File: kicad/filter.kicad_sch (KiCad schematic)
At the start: 21 parts, among them Q19 BC547, Q20 BC557, U1 NE5532

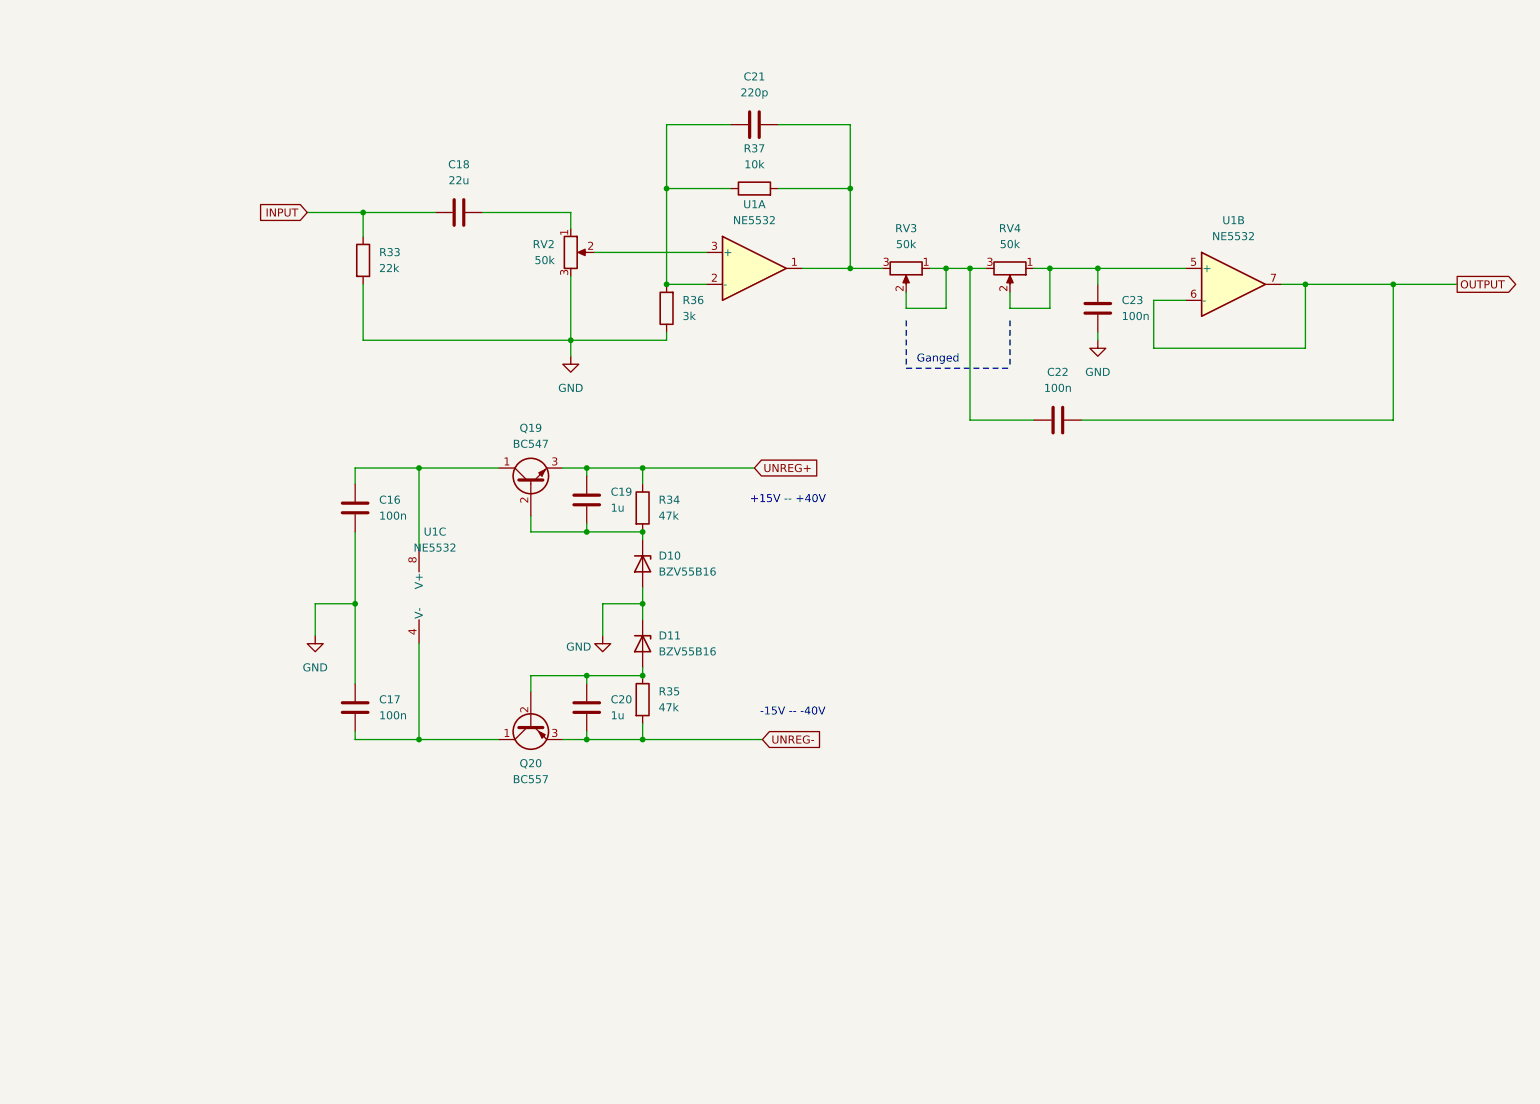
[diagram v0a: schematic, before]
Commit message: Added preamp sim
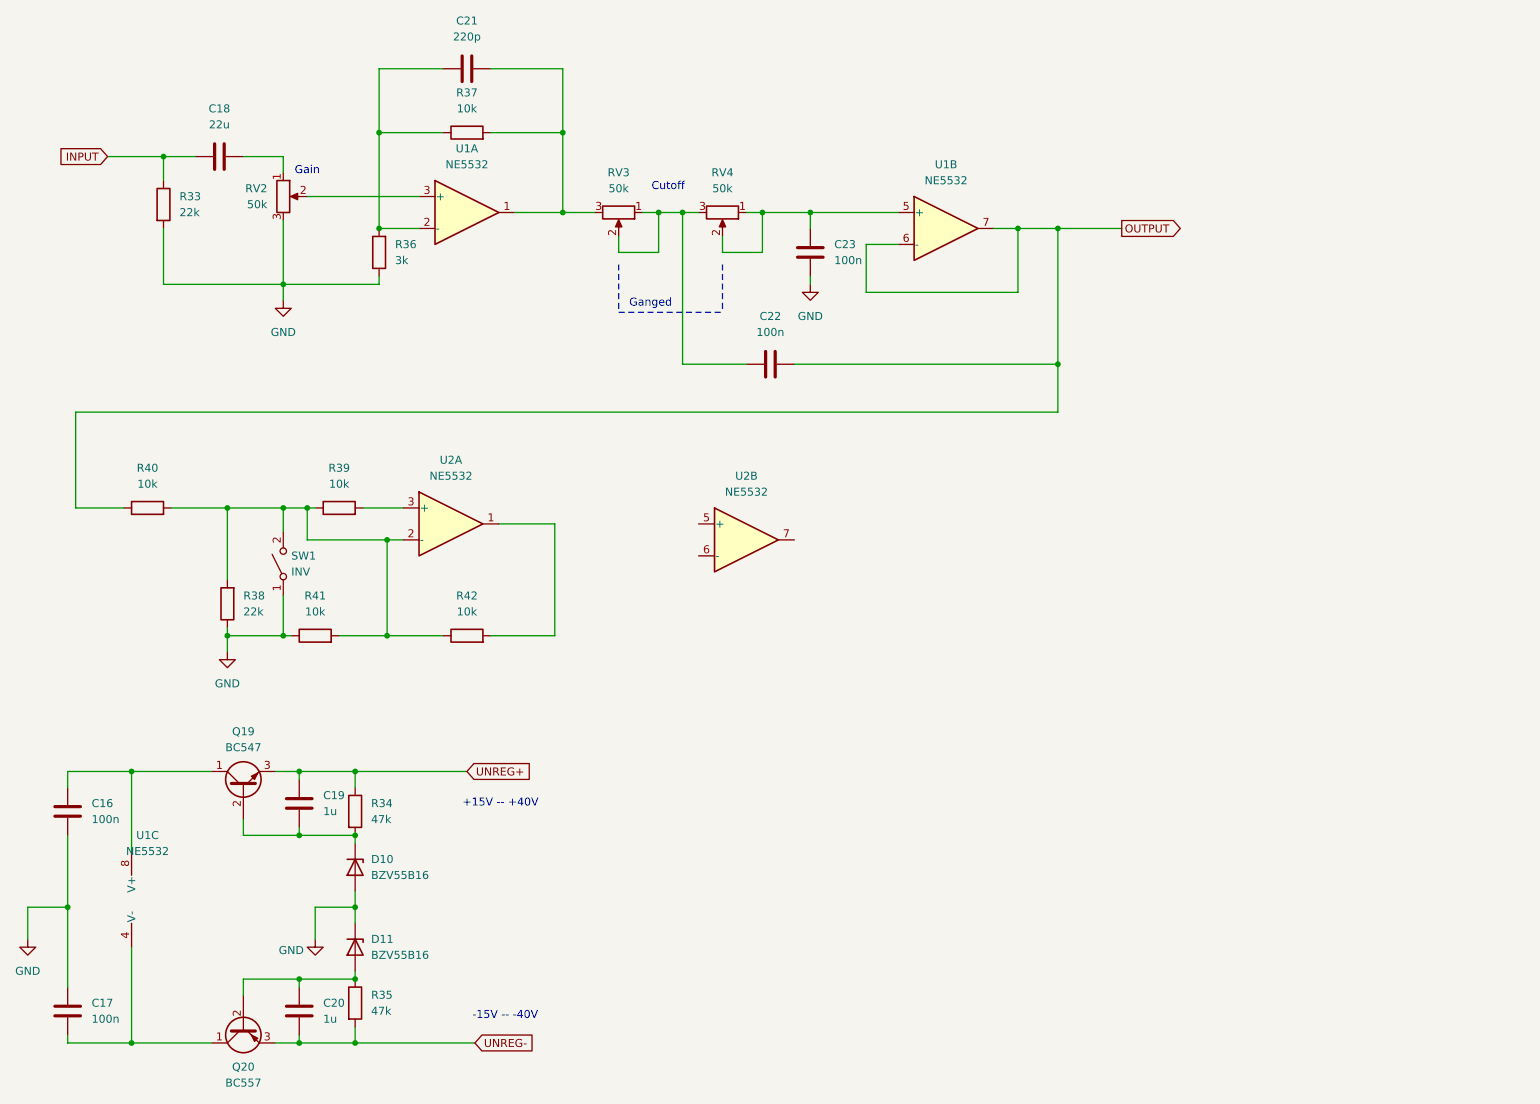
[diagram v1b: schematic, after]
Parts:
- added R38: 22k, Resistor_THT:R_Axial_DIN0204_L3.6mm_D1.6mm_P7.62mm_Horizontal, symbol Device:R
- added R39, R40, R41, R42: 10k, Resistor_THT:R_Axial_DIN0204_L3.6mm_D1.6mm_P7.62mm_Horizontal, symbol Device:R
- added SW1: INV, symbol Switch:SW_SPST
- added U2: NE5532, Package_DIP:DIP-8_W7.62mm, symbol Amplifier_Operational:NE5532
- C16, C17, C21, C22, C23: footprint (none) -> Capacitor_THT:C_Rect_L7.2mm_W3.0mm_P5.00mm_FKS2_FKP2_MKS2_MKP2
- C18, C19, C20: footprint (none) -> Capacitor_THT:CP_Radial_D4.0mm_P2.00mm
- R33, R34, R35, R36, R37, RV2, RV3, RV4: footprint (none) -> Resistor_THT:R_Axial_DIN0204_L3.6mm_D1.6mm_P7.62mm_Horizontal
- U1: footprint (none) -> Package_DIP:DIP-8_W7.62mm
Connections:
- net GND: now also R38.1, R41.1, SW1.1 (A)
- net OUTPUT: now also R40.1
- new net: R38.2, R39.1, R40.2, R41.2, R42.1, SW1.2 (B), U2.2 (-)
- new net: R42.2, U2.1
- new net: R39.2, U2.3 (+)
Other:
- note added: "Cutoff"
- note added: "Gain"
- moved on the sheet: C16, C17, C18, C19, C20, C21, C22, C23, D10, D11, Q19, Q20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

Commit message: WIP
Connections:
- net GND: now also C19.2, C20.1
- net UNREG+: no longer C19.1
- net UNREG-: no longer C20.2
- net at D11.2 (A), Q20.2 (B), R35.1: now also C20.2; no longer C20.1
- net at D10.1 (K), Q19.2 (B), R34.2: now also C19.1; no longer C19.2
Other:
- moved on the sheet: C19, C20

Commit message: WIP
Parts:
- removed C16, C17, C22, C23: 100n, Capacitor_THT:C_Rect_L7.2mm_W3.0mm_P5.00mm_FKS2_FKP2_MKS2_MKP2, symbol Device:C
- removed C18: 22u, Capacitor_THT:CP_Radial_D4.0mm_P2.00mm, symbol Device:C
- removed C19, C20: 1u, Capacitor_THT:CP_Radial_D4.0mm_P2.00mm, symbol Device:C
- removed C21: 220p, Capacitor_THT:C_Rect_L7.2mm_W3.0mm_P5.00mm_FKS2_FKP2_MKS2_MKP2, symbol Device:C
- removed D10, D11: BZV55B16, Diode_SMD:D_MiniMELF, symbol Diode:BZV55B16
- removed Q19: BC547, Package_TO_SOT_THT:TO-92_Inline, symbol Transistor_BJT:BC547
- removed Q20: BC557, Package_TO_SOT_THT:TO-92_Inline, symbol Transistor_BJT:BC557
- removed R33, R38: 22k, Resistor_THT:R_Axial_DIN0204_L3.6mm_D1.6mm_P7.62mm_Horizontal, symbol Device:R
- removed R34, R35: 47k, Resistor_THT:R_Axial_DIN0204_L3.6mm_D1.6mm_P7.62mm_Horizontal, symbol Device:R
- removed R36: 3k, Resistor_THT:R_Axial_DIN0204_L3.6mm_D1.6mm_P7.62mm_Horizontal, symbol Device:R
- removed R37, R39, R40, R41, R42: 10k, Resistor_THT:R_Axial_DIN0204_L3.6mm_D1.6mm_P7.62mm_Horizontal, symbol Device:R
- removed RV2, RV3, RV4: 50k, Resistor_THT:R_Axial_DIN0204_L3.6mm_D1.6mm_P7.62mm_Horizontal, symbol Device:R_Potentiometer
- removed SW1: INV, symbol Switch:SW_SPST
- removed U1, U2: NE5532, Package_DIP:DIP-8_W7.62mm, symbol Amplifier_Operational:NE5532
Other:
- note removed: "+15V -- +40V"
- note removed: "-15V -- -40V"
- note removed: "Cutoff"
- note removed: "Gain"
- note removed: "Ganged"
